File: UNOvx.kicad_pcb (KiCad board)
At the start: 2 copper layers, 72 x 53.5 mm, 35 parts, among them IC1 BTS462T, J1 Barrel_Jack_Switch, J2 I2C/TWI, J3 Conn_01x02_Male, J4 Conn_02x03_Odd_Even, P1 Analog PC, P2 Power, P3 Digital PB, P4 Digital PD, P5 CONN_01X01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

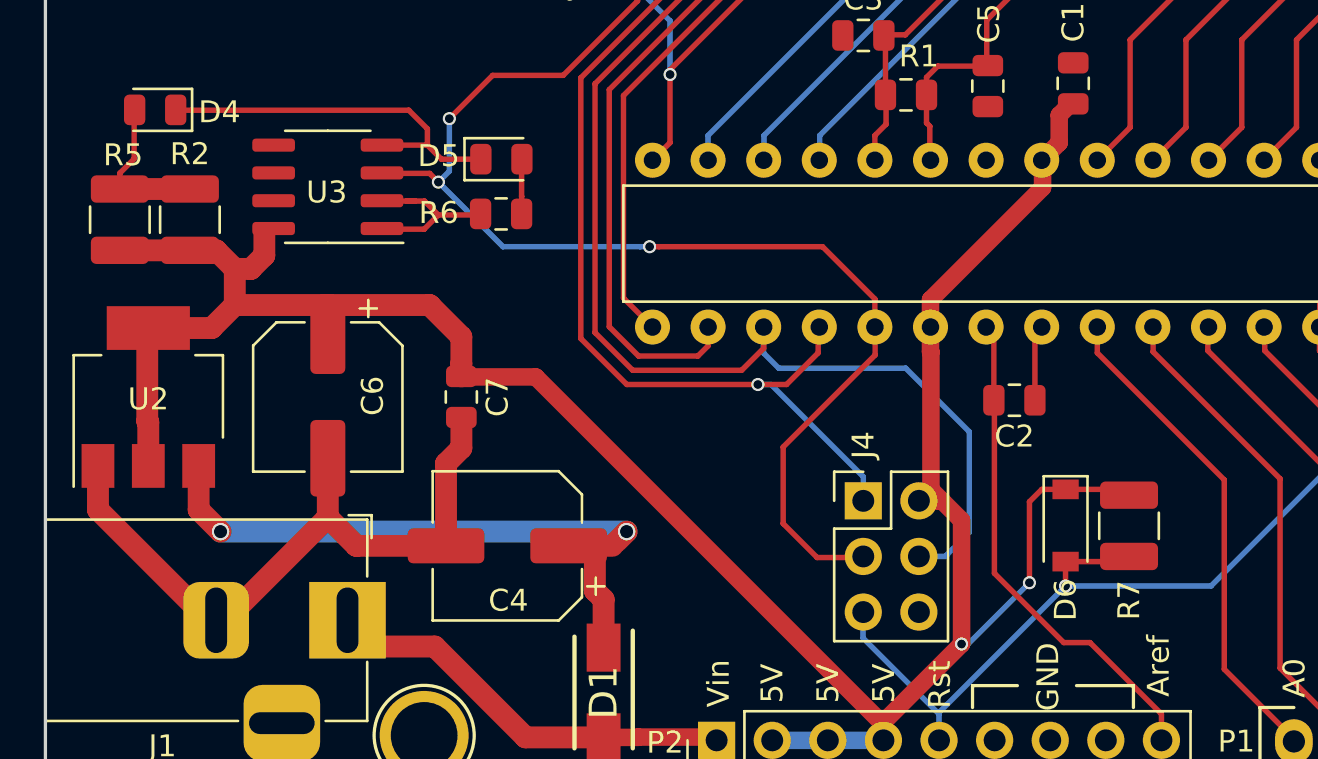
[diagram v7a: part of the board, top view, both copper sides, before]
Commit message: Update packages to 0805
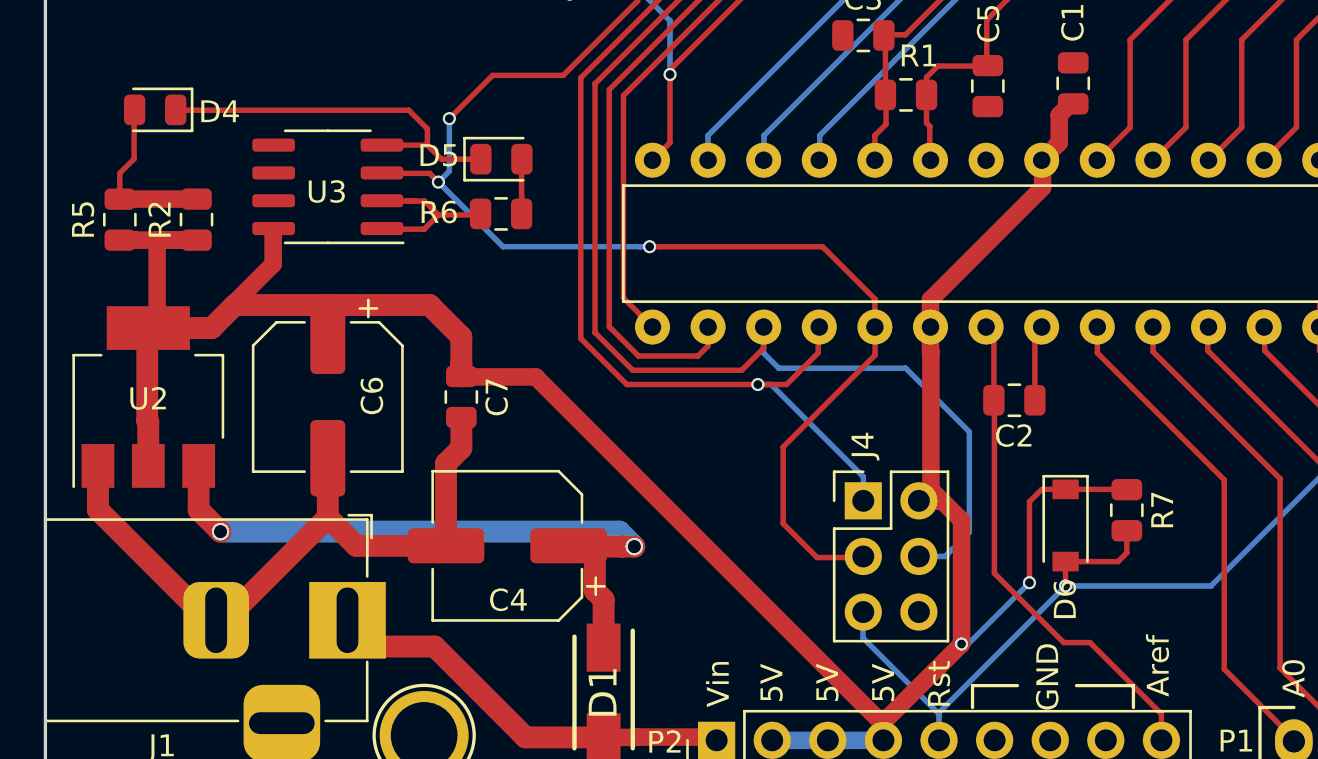
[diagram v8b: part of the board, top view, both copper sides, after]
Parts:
- added REF**: KiCad-Logo2_5mm_SilkScreen, Symbol:KiCad-Logo2_5mm_SilkScreen, B.Cu at (123.9, 107.5)
- R2, R5: footprint Capacitor_SMD:C_1210_3225Metric -> Resistor_SMD:R_0805_2012Metric
- R7: footprint Resistor_SMD:R_1210_3225Metric -> Resistor_SMD:R_0805_2012Metric
- moved R7 0.72 mm to (157.1, 113.5)
- moved R2 0.30 mm to (114.6, 100.3)
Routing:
- net +5V: track 111.7 -> 116.5 mm
- net Reset: track 64.7 -> 66.1 mm
- net Net-(C4-Pad1): track 29.4 -> 28.6 mm
